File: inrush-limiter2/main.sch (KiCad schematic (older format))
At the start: 32 parts, among them K1 RELAY_2RT, P1 CONN_01X04, P2 CONN_01X02, Q1 2N3904, Q2 PN2222A, T1 MY-TRANSFO, U1 LM393, U2 50 ohm NTC

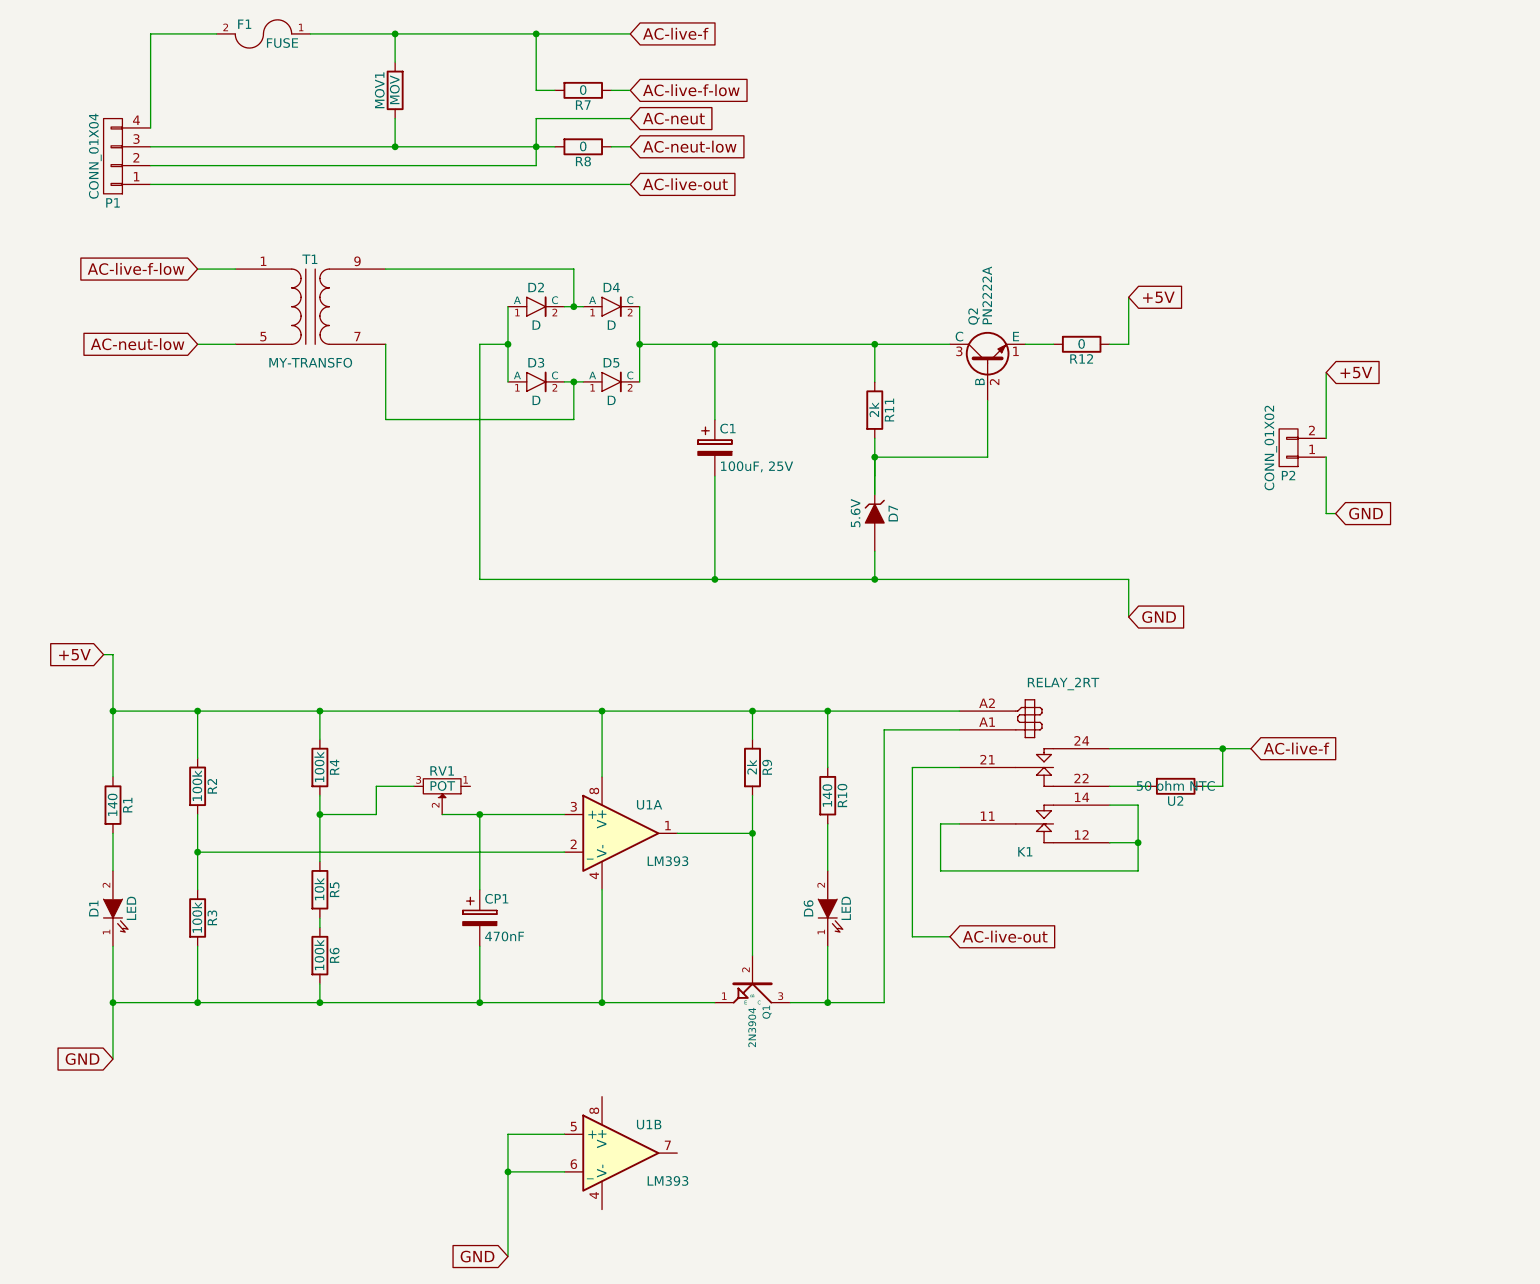
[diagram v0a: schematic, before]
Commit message: fixed with a resistor but not sure its necessary
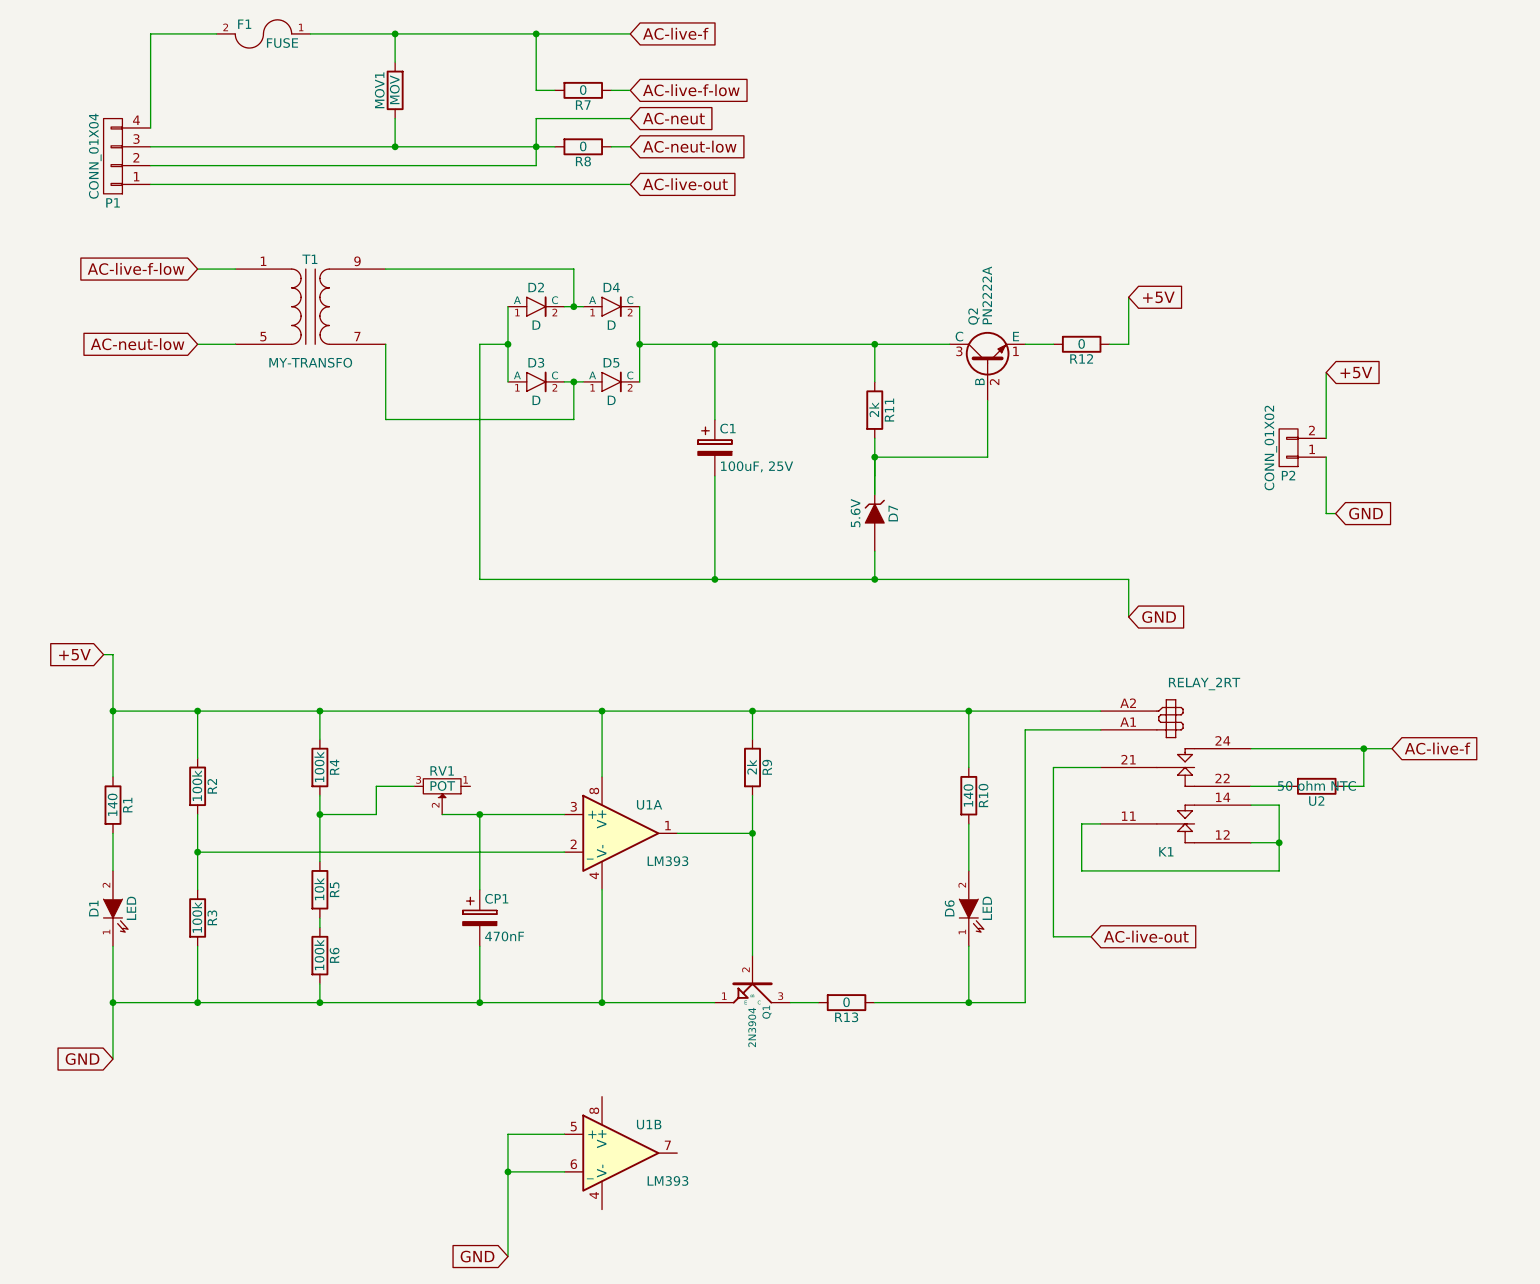
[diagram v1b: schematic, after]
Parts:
- added R13: 0, symbol R
- T1: footprint (none) -> test:my-transformer
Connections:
- net at D6.1 (K), K1.A1 (8): now also R13.1; no longer Q1.3 (C)
- new net: Q1.3 (C), R13.2
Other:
- moved on the sheet: D6, K1, R10, U2
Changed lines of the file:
@@
 Text GLabel 3900 750  2    60   Input ~ 0
 AC-live-f
-Text GLabel 5600 5550 2    60   Input ~ 0
+Text GLabel 6350 5550 2    60   Input ~ 0
 AC-live-out
 $Comp
 L RELAY_2RT K1
 U 1 1 57C3B514
-P 6050 4700
-F 0 "K1" H 6000 5100 50  0000 C CNN
-F 1 "RELAY_2RT" H 6200 4200 50  0000 C CNN
-F 2 "Relays_ThroughHole:Relay_DPDT_Schrack-RT2_RM5mm" H 6050 4700 50  0001 C CNN
-F 3 "" H 6050 4700 50  0000 C CNN
-	1    6050 4700
+P 6800 4700
+F 0 "K1" H 6750 5100 50  0000 C CNN
+F 1 "RELAY_2RT" H 6950 4200 50  0000 C CNN
+F 2 "Relays_ThroughHole:Relay_DPDT_Schrack-RT2_RM5mm" H 6800 4700 50  0001 C CNN
+F 3 "" H 6800 4700 50  0000 C CNN
+	1    6800 4700
 	1    0    0    1
 $EndComp
@@
 L LED D6
 U 1 1 57CC7BFD
-P 4950 5400
-F 0 "D6" H 4950 5500 50  0000 C CNN
-F 1 "LED" H 4950 5300 50  0000 C CNN
-F 2 "LEDs:LED-5MM" H 4950 5400 50  0001 C CNN
-F 3 "" H 4950 5400 50  0000 C CNN
-	1    4950 5400
+P 5700 5400
+F 0 "D6" H 5700 5500 50  0000 C CNN
+F 1 "LED" H 5700 5300 50  0000 C CNN
+F 2 "LEDs:LED-5MM" H 5700 5400 50  0001 C CNN
+F 3 "" H 5700 5400 50  0000 C CNN
+	1    5700 5400
 	0    -1   -1   0
 $EndComp
@@
 L R R10
 U 1 1 57CC7DA4
-P 4950 4800
-F 0 "R10" V 5030 4800 50  0000 C CNN
-F 1 "140" V 4950 4800 50  0000 C CNN
-F 2 "Resistors_ThroughHole:Resistor_Horizontal_RM7mm" V 4880 4800 50  0001 C CNN
-F 3 "" H 4950 4800 50  0000 C CNN
-	1    4950 4800
-	1    0    0    -1
-$EndComp
-Text GLabel 7200 4550 2    60   Input ~ 0
+P 5700 4800
+F 0 "R10" V 5780 4800 50  0000 C CNN
+F 1 "140" V 5700 4800 50  0000 C CNN
+F 2 "Resistors_ThroughHole:Resistor_Horizontal_RM7mm" V 5630 4800 50  0001 C CNN
+F 3 "" H 5700 4800 50  0000 C CNN
+	1    5700 4800
+	1    0    0    -1
+$EndComp
+Text GLabel 7950 4550 2    60   Input ~ 0
 AC-live-f
 $Comp
 L R U2
 U 1 1 57CC96A4
-P 6800 4750
-F 0 "U2" V 6880 4750 50  0000 C CNN
-F 1 "50 ohm NTC" V 6800 4750 50  0000 C CNN
-F 2 "Resistors_ThroughHole:Resistor_Horizontal_RM10mm" V 6730 4750 50  0001 C CNN
-F 3 "" H 6800 4750 50  0000 C CNN
-	1    6800 4750
+P 7550 4750
+F 0 "U2" V 7630 4750 50  0000 C CNN
+F 1 "50 ohm NTC" V 7550 4750 50  0000 C CNN
+F 2 "Resistors_ThroughHole:Resistor_Horizontal_RM10mm" V 7480 4750 50  0001 C CNN
+F 3 "" H 7550 4750 50  0000 C CNN
+	1    7550 4750
 	0    1    1    0
 $EndComp
@@
 	3550 6600 3250 6600
 Wire Wire Line
-	6650 4750 6450 4750
-Connection ~ 7050 4550
-Wire Wire Line
-	7050 4750 6950 4750
-Wire Wire Line
-	7050 4550 7050 4750
-Wire Wire Line
-	6450 4550 7200 4550
+	7400 4750 7200 4750
+Connection ~ 7800 4550
+Wire Wire Line
+	7800 4750 7700 4750
+Wire Wire Line
+	7800 4550 7800 4750
+Wire Wire Line
+	7200 4550 7950 4550
 Wire Wire Line
 	6550 3650 6550 3850
@@
 	1600 2000 1800 2000
 Wire Wire Line
-	5250 5900 5250 4450
-Wire Wire Line
-	5250 4450 5650 4450
-Connection ~ 4950 5900
-Wire Wire Line
-	4950 5600 4950 5900
-Wire Wire Line
-	4950 4950 4950 5200
-Connection ~ 4950 4350
-Wire Wire Line
-	4950 4350 4950 4650
+	6000 5900 6000 4450
+Wire Wire Line
+	6000 4450 6400 4450
+Connection ~ 5700 5900
+Wire Wire Line
+	5700 5600 5700 5900
+Wire Wire Line
+	5700 4950 5700 5200
+Connection ~ 5700 4350
+Wire Wire Line
+	5700 4350 5700 4650
 Wire Wire Line
 	4550 5000 4150 5000
@@
 	4550 4350 4550 4500
 Wire Wire Line
-	4750 5900 5250 5900
+	5200 5900 6000 5900
 Wire Wire Line
 	4550 4800 4550 5650
@@
 	1150 4050 1150 4700
 Wire Wire Line
-	5400 5550 5600 5550
-Wire Wire Line
-	5400 4650 5400 5550
-Wire Wire Line
-	5650 4650 5400 4650
+	6150 5550 6350 5550
+Wire Wire Line
+	6150 4650 6150 5550
+Wire Wire Line
+	6400 4650 6150 4650
 Connection ~ 3750 5900
 Connection ~ 3100 4900
@@
 	1350 1550 3900 1550
 Wire Wire Line
-	1150 4350 5650 4350
+	1150 4350 6400 4350
 Connection ~ 4350 2400
 Wire Wire Line
@@
 Connection ~ 3750 4350
 Wire Wire Line
-	5650 4950 5550 4950
-Wire Wire Line
-	5550 4950 5550 5200
-Wire Wire Line
-	6600 5200 5550 5200
-Wire Wire Line
-	6600 4850 6600 5200
-Wire Wire Line
-	6600 4850 6450 4850
-Wire Wire Line
-	6450 5050 6600 5050
-Connection ~ 6600 5050
+	6400 4950 6300 4950
+Wire Wire Line
+	6300 4950 6300 5200
+Wire Wire Line
+	6300 5200 7350 5200
+Wire Wire Line
+	7350 5200 7350 4850
+Wire Wire Line
+	7350 4850 7200 4850
+Wire Wire Line
+	7200 5050 7350 5050
+Connection ~ 7350 5050
 Wire Wire Line
 	2250 4500 2250 4350
@@
 F 0 "T1" H 2200 2450 50  0000 C CNN
 F 1 "MY-TRANSFO" H 2200 1900 50  0000 C CNN
-F 2 "" H 2200 2200 50  0000 C CNN
+F 2 "test:my-transformer" H 2200 2200 50  0001 C CNN
 F 3 "" H 2200 2200 50  0000 C CNN
 	1    2200 2200
 	1    0    0    -1
 $EndComp
+$Comp
+L R R13
+U 1 1 57D05B30
+P 5050 5900
+F 0 "R13" V 5130 5900 50  0000 C CNN
+F 1 "0" V 5050 5900 50  0000 C CNN
+F 2 "" V 4980 5900 50  0000 C CNN
+F 3 "" H 5050 5900 50  0000 C CNN
+	1    5050 5900
+	0    1    1    0
+$EndComp
+Wire Wire Line
+	4900 5900 4750 5900
 $EndSCHEMATC

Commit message: yes its needed
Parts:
- R13: footprint (none) -> Resistors_ThroughHole:Resistor_Horizontal_RM7mm

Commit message: more tidying
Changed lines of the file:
@@
 	3250 6800 3550 6800
 Wire Wire Line
-	3250 6600 3250 6800
-Wire Wire Line
-	3250 6800 3250 7250
+	3250 6600 3250 7250
 Wire Wire Line
 	3550 6600 3250 6600
@@
 	7800 4550 7800 4750
 Wire Wire Line
-	7200 4550 7800 4550
-Wire Wire Line
-	7800 4550 7950 4550
+	7200 4550 7950 4550
 Wire Wire Line
 	6550 3650 6550 3850
@@
 	4550 4350 4550 4500
 Wire Wire Line
-	5200 5900 5700 5900
+	5200 5900 6000 5900
 Wire Wire Line
-	5700 5900 6000 5900
-Wire Wire Line
-	4550 4800 4550 5000
-Wire Wire Line
-	4550 5000 4550 5650
+	4550 4800 4550 5650
 Connection ~ 1150 4350
 Connection ~ 1150 5900
 Wire Wire Line
-	1150 5600 1150 5900
+	1150 5600 1150 6200
 Wire Wire Line
-	1150 5900 1150 6200
-Wire Wire Line
-	1150 4050 1150 4350
-Wire Wire Line
-	1150 4350 1150 4700
+	1150 4050 1150 4700
 Wire Wire Line
 	6150 5550 6350 5550
@@
 	3100 4900 3100 5300
 Wire Wire Line
-	2900 4900 3100 4900
-Wire Wire Line
-	3100 4900 3550 4900
+	2900 4900 3550 4900
 Connection ~ 2250 4900
 Wire Wire Line
 	2250 4900 2550 4900
 Wire Wire Line
-	2250 4800 2250 4900
+	2250 4800 2250 5150
 Wire Wire Line
-	2250 4900 2250 5150
-Wire Wire Line
-	1600 4900 1600 5100
-Wire Wire Line
-	1600 5100 1600 5300
+	1600 4900 1600 5300
 Wire Wire Line
 	2250 5450 2250 5500
@@
 	5200 3650 5200 3500
 Wire Wire Line
-	1150 5900 1600 5900
-Wire Wire Line
-	1600 5900 2250 5900
-Wire Wire Line
-	2250 5900 3100 5900
-Wire Wire Line
-	3100 5900 3750 5900
-Wire Wire Line
-	3750 5900 4350 5900
+	1150 5900 4350 5900
 Connection ~ 1600 4350
 Wire Wire Line
 	1600 4350 1600 4600
 Wire Wire Line
-	5200 2900 5200 3000
-Wire Wire Line
-	5200 3000 5200 3100
+	5200 2900 5200 3100
 Wire Wire Line
 	5200 3000 5200 3200
@@
 Connection ~ 3400 750
 Wire Wire Line
-	2200 750  2650 750
-Wire Wire Line
-	2650 750  3400 750
-Wire Wire Line
-	3400 750  3900 750
+	2200 750  3900 750
 Wire Wire Line
 	3800 1050 3900 1050
 Connection ~ 3400 1350
 Wire Wire Line
-	3400 1200 3400 1350
-Wire Wire Line
-	3400 1350 3400 1450
+	3400 1200 3400 1450
 Wire Wire Line
 	3800 1350 3900 1350
 Wire Wire Line
-	1350 1350 2650 1350
-Wire Wire Line
-	2650 1350 3400 1350
-Wire Wire Line
-	3400 1350 3500 1350
+	1350 1350 3500 1350
 Wire Wire Line
 	3900 1200 3400 1200
@@
 	1350 1550 3900 1550
 Wire Wire Line
-	1150 4350 1600 4350
-Wire Wire Line
-	1600 4350 2250 4350
-Wire Wire Line
-	2250 4350 3750 4350
-Wire Wire Line
-	3750 4350 4550 4350
-Wire Wire Line
-	4550 4350 5700 4350
-Wire Wire Line
-	5700 4350 6400 4350
+	1150 4350 6400 4350
 Connection ~ 4350 2400
 Wire Wire Line
@@
 Connection ~ 3950 2400
 Wire Wire Line
-	3950 2400 4350 2400
-Wire Wire Line
-	4350 2400 5200 2400
-Wire Wire Line
-	5200 2400 5600 2400
+	3950 2400 5600 2400
 Connection ~ 3250 2400
 Wire Wire Line
@@
 	3600 2800 3600 2600
 Wire Wire Line
-	3550 2600 3600 2600
+	3550 2600 3650 2600
 Wire Wire Line
-	3600 2600 3650 2600
+	3950 2200 3950 2600
 Wire Wire Line
-	3950 2200 3950 2400
-Wire Wire Line
-	3950 2400 3950 2600
-Wire Wire Line
-	3250 2200 3250 2400
-Wire Wire Line
-	3250 2400 3250 2600
+	3250 2200 3250 2600
 Connection ~ 3600 2200
 Wire Wire Line
-	3550 2200 3600 2200
-Wire Wire Line
-	3600 2200 3650 2200
+	3550 2200 3650 2200
 Wire Wire Line
 	3600 2000 3600 2200
 Wire Wire Line
-	3100 3650 4350 3650
-Wire Wire Line
-	4350 3650 5200 3650
-Wire Wire Line
-	5200 3650 6550 3650
+	3100 3650 6550 3650
 Connection ~ 4350 3650
 Wire Wire Line
@@
 	6300 4950 6300 5200
 Wire Wire Line
-	6300 5200 7350 5200
+	7350 5200 6300 5200
 Wire Wire Line
-	7350 5200 7350 5050
-Wire Wire Line
-	7350 5050 7350 4850
+	7350 4850 7350 5200
 Wire Wire Line
 	7350 4850 7200 4850
